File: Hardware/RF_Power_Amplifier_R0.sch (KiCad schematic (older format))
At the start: 1 part

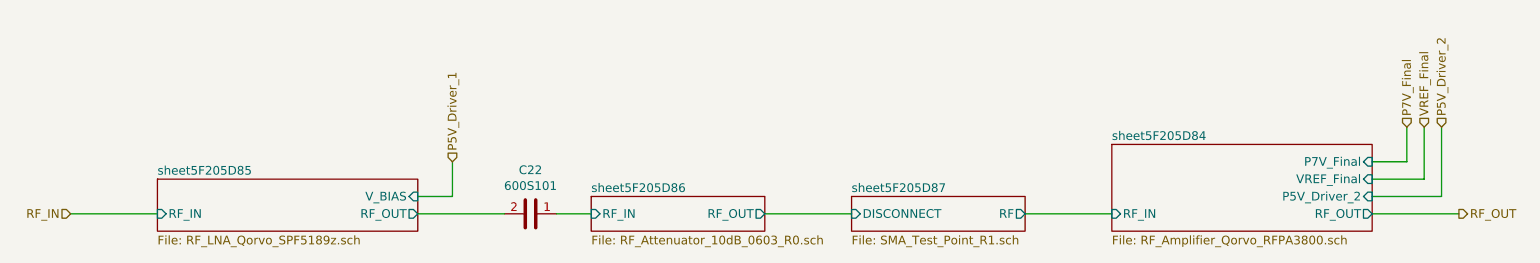
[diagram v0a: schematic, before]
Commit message: Improving LNA simulations and Documentation package. More to come on this one.
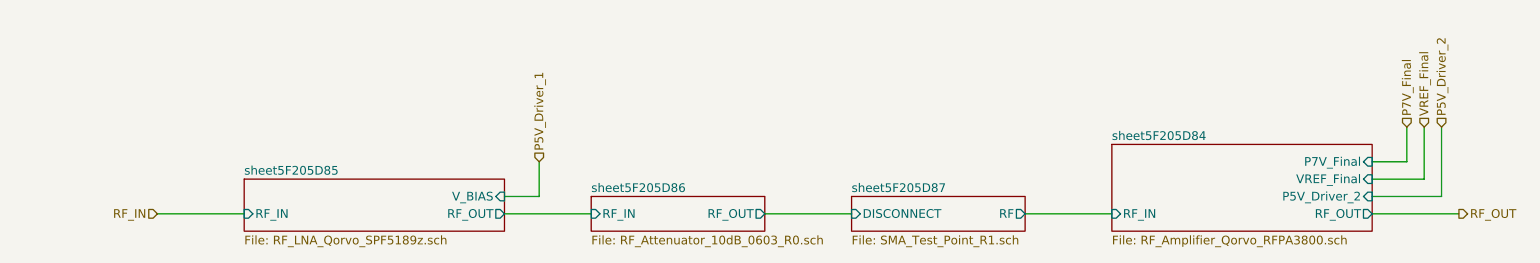
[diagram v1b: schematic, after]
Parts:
- removed C22: 600S101, Capacitor_SMD:C_0603_1608Metric, symbol ATC:600S101
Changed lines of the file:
@@
 $Descr A4 11693 8268
 encoding utf-8
-Sheet 14 24
+Sheet 14 23
 Title ""
 Date ""
@@
 $EndSheet
 $Sheet
-S 2500 3700 1500 300
+S 3000 3700 1500 300
 U 5F205D93
 F0 "sheet5F205D85" 50
 F1 "RF_LNA_Qorvo_SPF5189z.sch" 50
-F2 "RF_IN" I L 2500 3900 50
-F3 "V_BIAS" I R 4000 3800 50
-F4 "RF_OUT" O R 4000 3900 50
+F2 "RF_IN" I L 3000 3900 50
+F3 "V_BIAS" I R 4500 3800 50
+F4 "RF_OUT" O R 4500 3900 50
 $EndSheet
 Wire Wire Line
@@
 F3 "RF" O R 7500 3900 50
 $EndSheet
-$Comp
-L ATC:600S101 C22
-U 1 1 5F205DA4
-P 4650 3900
-F 0 "C22" V 4398 3900 50  0000 C CNN
-F 1 "600S101" V 4489 3900 50  0000 C CNN
-F 2 "Capacitor_SMD:C_0603_1608Metric" H 4700 4000 50  0001 C CNN
-F 3 "" H 4700 4000 50  0001 C CNN
-	1    4650 3900
-	0    1    1    0
-$EndComp
-Wire Wire Line
-	4800 3900 5000 3900
-Wire Wire Line
-	4000 3900 4500 3900
 Wire Wire Line
 	6000 3900 6500 3900
-Text HLabel 2000 3900 0    50   Input ~ 0
+Text HLabel 2500 3900 0    50   Input ~ 0
 RF_IN
 Text HLabel 10000 3900 2    50   Output ~ 0
@@
 	10000 3900 9500 3900
 Wire Wire Line
-	2000 3900 2500 3900
+	2500 3900 3000 3900
 Wire Wire Line
-	4000 3800 4200 3800
+	4500 3800 4700 3800
 Wire Wire Line
-	4200 3800 4200 3600
-Text HLabel 4200 3600 1    50   Input ~ 0
+	4700 3800 4700 3600
+Text HLabel 4700 3600 1    50   Input ~ 0
 P5V_Driver_1
 Wire Wire Line
@@
 Text HLabel 9800 3400 1    50   Input ~ 0
 VREF_Final
+Wire Wire Line
+	4500 3900 5000 3900
 $EndSCHEMATC
